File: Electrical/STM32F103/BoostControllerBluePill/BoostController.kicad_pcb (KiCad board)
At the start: 2 copper layers, 81.8 x 80 mm, 57 parts, among them J1 PW-RPM-SPD-TPS, J2 OIL-WATER-AFR, J3 WG-FPUMP, J4 MAP-FPRES, J5 CAN, J6 GND_TP, J7 PROG, Q1 IRF540N, Q2 IRF540N, Q3 BC337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

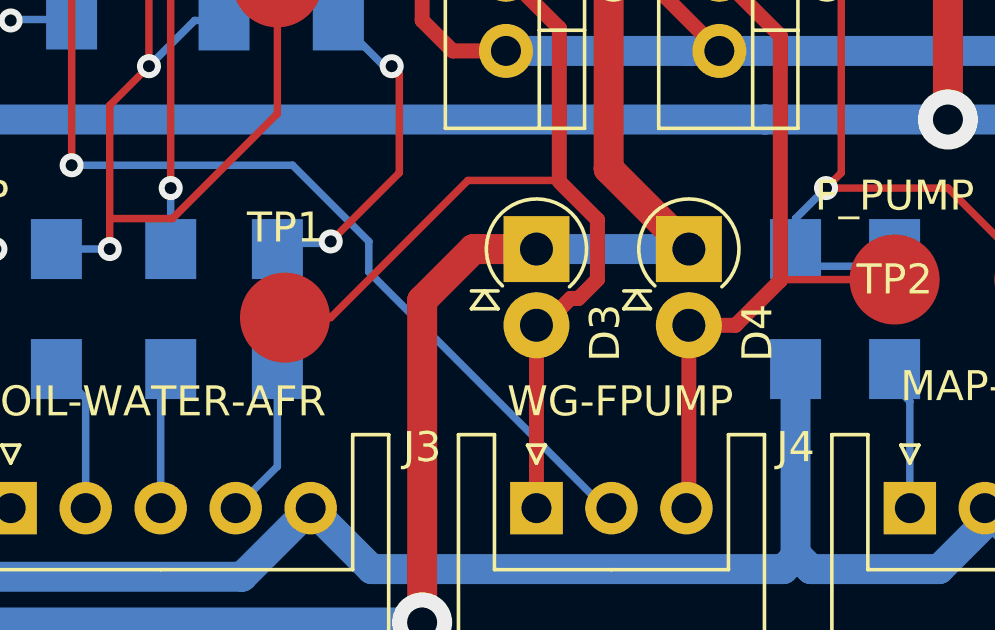
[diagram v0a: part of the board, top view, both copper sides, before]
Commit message: PCB rev 1.1 Fixed track width for solenoid and relay driver Removed spurious hole Cleared overwrites in fab layer Fixed missing name on WG_SOL TP
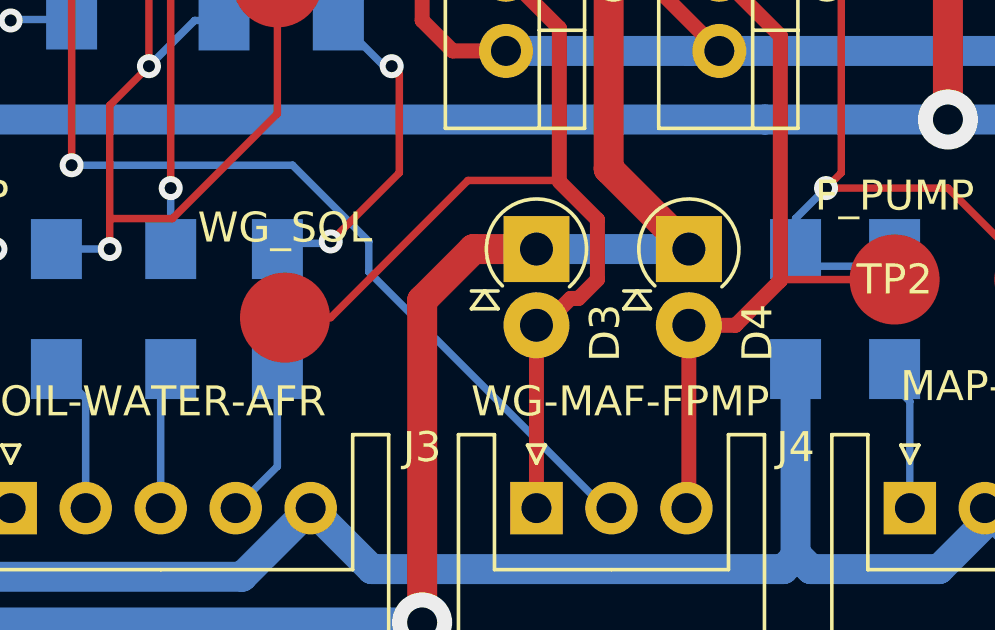
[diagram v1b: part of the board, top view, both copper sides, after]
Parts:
- J3: value WG-FPUMP -> WG-MAF-FPMP
- renumbered TP1 to WG_SOL

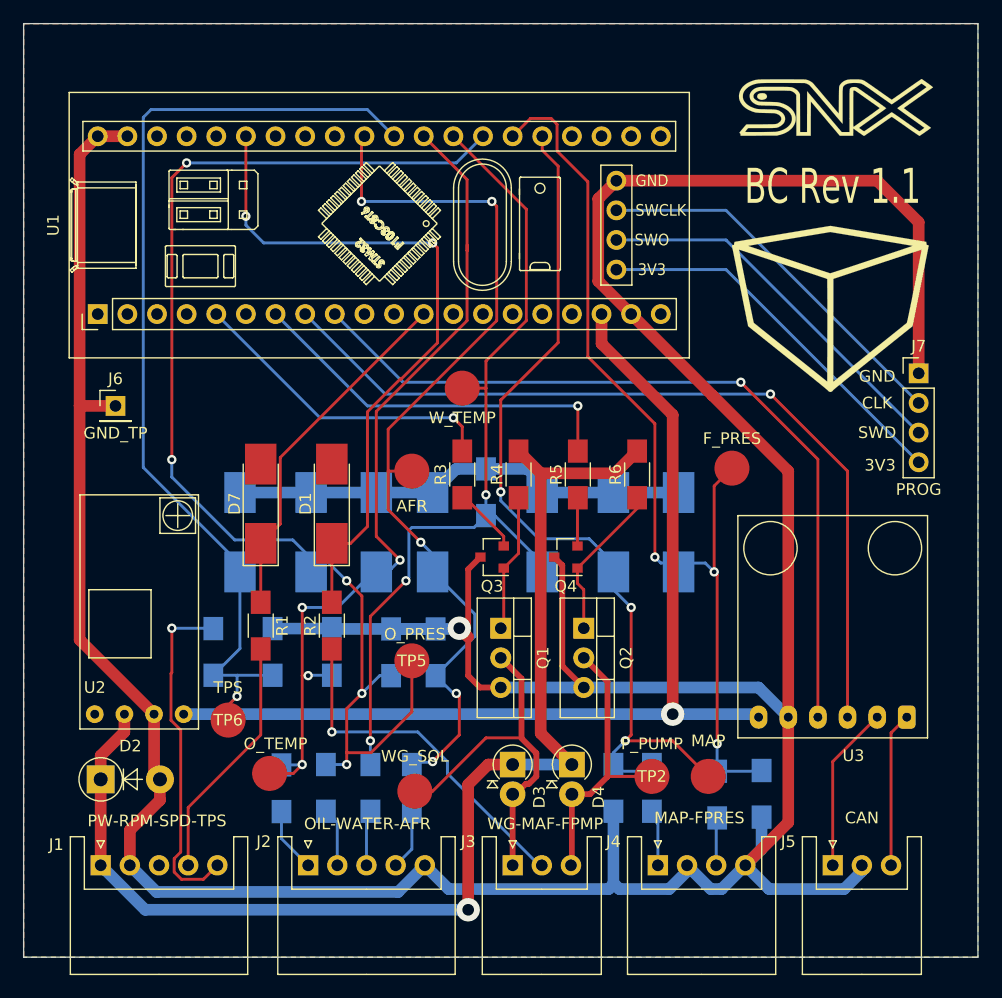
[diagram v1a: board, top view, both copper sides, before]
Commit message: PCB rev 1.2 Fixed missing RPM input Ported to Kicad 6 Fixed DRC warning on silkscreen
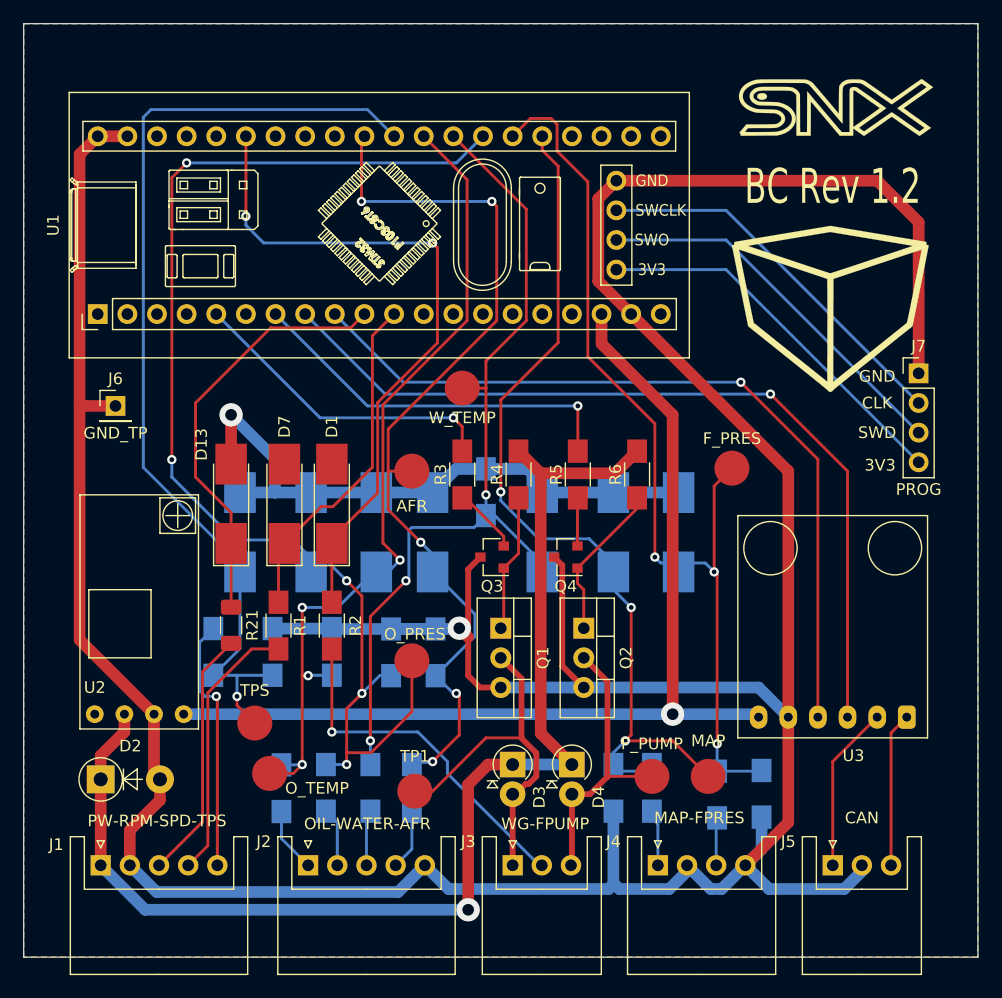
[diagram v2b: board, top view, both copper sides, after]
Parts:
- added D13: 3.3V, Diode_SMD:D_MELF_Handsoldering, F.Cu at (76.2, 85.6)
- added R21: 4.7k, Resistor_SMD:R_1206_3216Metric_Pad1.30x1.75mm_HandSolder, F.Cu at (76.2, 96.0)
- J3: value WG-MAF-FPMP -> WG-FPUMP
- moved TP6 2.30 mm to (78.2, 104.4)
- moved D7 2.03 mm to (80.8, 85.6)
- moved R1 1.52 mm to (80.3, 96.0)
- renumbered WG_SOL to TP1
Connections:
- J1 pad 3: (no net) -> /RPM
- U1 pad 1: (no net) -> unconnected-(U1-Pad1)
- U1 pad 10: (no net) -> Net-(U1-Pad10)
- U1 pad 11: (no net) -> Net-(D7-Pad1)
- U1 pad 12: Net-(D7-Pad1) -> unconnected-(U1-Pad12)
- U1 pad 13: (no net) -> unconnected-(U1-Pad13)
- U1 pad 14: (no net) -> unconnected-(U1-Pad14)
- U1 pad 15: (no net) -> unconnected-(U1-Pad15)
- U1 pad 16: (no net) -> unconnected-(U1-Pad16)
- U1 pad 17: (no net) -> unconnected-(U1-Pad17)
- U1 pad 2: (no net) -> unconnected-(U1-Pad2)
- U1 pad 20: (no net) -> unconnected-(U1-Pad20)
- U1 pad 21: (no net) -> unconnected-(U1-Pad21)
- U1 pad 22: (no net) -> unconnected-(U1-Pad22)
- U1 pad 23: (no net) -> unconnected-(U1-Pad23)
- U1 pad 24: (no net) -> unconnected-(U1-Pad24)
- U1 pad 3: (no net) -> unconnected-(U1-Pad3)
- U1 pad 32: (no net) -> unconnected-(U1-Pad32)
- U1 pad 33: (no net) -> unconnected-(U1-Pad33)
- U1 pad 34: (no net) -> unconnected-(U1-Pad34)
- U1 pad 36: (no net) -> unconnected-(U1-Pad36)
- U1 pad 37: (no net) -> unconnected-(U1-Pad37)
- U1 pad 38: (no net) -> unconnected-(U1-Pad38)
- U1 pad 4: (no net) -> unconnected-(U1-Pad4)
- U1 pad 6: (no net) -> unconnected-(U1-Pad6)
- U2 pad 4: (no net) -> unconnected-(U2-Pad4)
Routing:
- net Net-(U1-Pad10): track 0.00 -> 36.4 mm
- net /RPM: track 0.00 -> 21.6 mm
- net GND: track 375.2 -> 387.6 mm, vias 1 -> 2
- net /TPS: track 29.5 -> 22.0 mm
- net /SPEED: track 21.1 -> 23.1 mm
- net Net-(D7-Pad1): track 30.5 -> 29.4 mm
- net /MAF_33: track 60.0 -> 59.0 mm
- net /OIL_TEMP_33: track 73.4 -> 72.4 mm
- net /TPS_33: track 84.2 -> 84.7 mm
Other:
- net class Default removed
- net class Power removed
- board text added: "BC Rev 1.2"
- board text removed: "BC Rev 1.1"

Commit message: Fixed SOT-23 transistors. Added test points. Changed footprint to Kicad6.
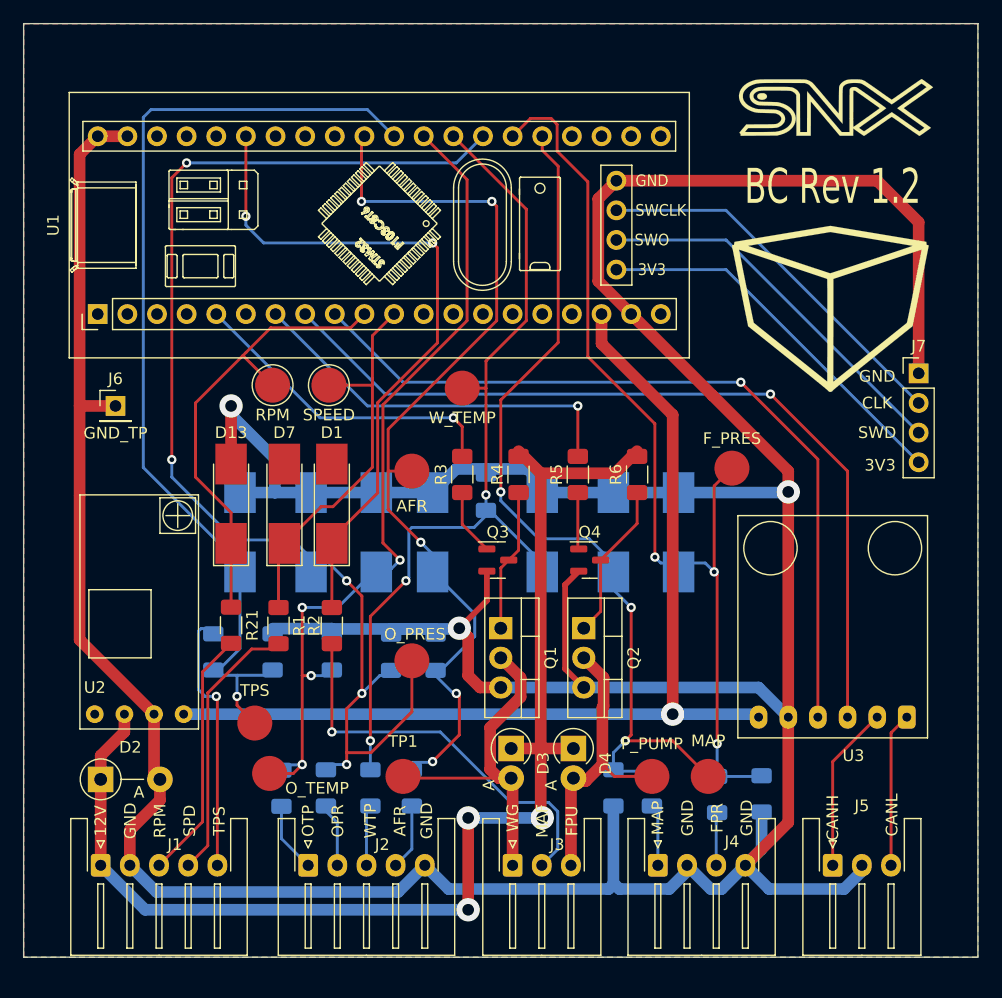
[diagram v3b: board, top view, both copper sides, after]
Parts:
- added TP10: RPM, TestPoint:TestPoint_Pad_D3.0mm, F.Cu at (79.8, 75.4)
- added TP11: SPEED, TestPoint:TestPoint_Pad_D3.0mm, F.Cu at (84.6, 75.4)
- D1, D10, D11, D5, D6, D7, D8, D9: footprint Diodes_SMD:D_MELF_Handsoldering -> Diode_SMD:D_MELF_Handsoldering
- D2: footprint Diodes_THT:D_DO-15_P5.08mm_Vertical_AnodeUp -> Diode_THT:D_DO-41_SOD81_P5.08mm_Vertical_AnodeUp
- D3, D4: footprint Diodes_THT:D_DO-41_SOD81_P2.54mm_Vertical_AnodeUp -> Diode_THT:D_DO-41_SOD81_P2.54mm_Vertical_AnodeUp
- J1, J2: footprint Connectors_JST:JST_XH_S05B-XH-A_05x2.50mm_Angled -> Connector_JST:JST_XH_S5B-XH-A-1_1x05_P2.50mm_Horizontal
- J3, J5: footprint Connectors_JST:JST_XH_S03B-XH-A_03x2.50mm_Angled -> Connector_JST:JST_XH_S3B-XH-A-1_1x03_P2.50mm_Horizontal
- J4: footprint Connectors_JST:JST_XH_S04B-XH-A_04x2.50mm_Angled -> Connector_JST:JST_XH_S4B-XH-A-1_1x04_P2.50mm_Horizontal
- J7: footprint Pin_Headers:Pin_Header_Straight_1x04_Pitch2.54mm -> Connector_PinHeader_2.54mm:PinHeader_1x04_P2.54mm_Vertical
- Q1, Q2: footprint TO_SOT_Packages_THT:TO-220-3_Vertical -> Package_TO_SOT_THT:TO-220-3_Vertical
- Q3, Q4: value BC337 -> S9013; footprint TO_SOT_Packages_SMD:SOT-23 -> Package_TO_SOT_SMD:SOT-23
- R1, R10, R11, R12, R13, R14, R15, R16, R17, R18, R19, R2, R20, R3, R4, R5, R6, R7, R8, R9: footprint Resistors_SMD:R_1206_HandSoldering -> Resistor_SMD:R_1206_3216Metric_Pad1.30x1.75mm_HandSolder
- moved Q4 2.06 mm to (106.9, 90.4), turned to 0 degrees
- moved TP1 1.63 mm to (90.9, 109.0)
- moved D4 1.38 mm to (105.5, 106.6)
- moved D3 1.38 mm to (100.2, 106.6)
- moved Q3 0.55 mm to (99.1, 90.4), turned to 0 degrees
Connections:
- Q3 pad 1: Net-(Q1-Pad1) -> Net-(R3-Pad1)
- Q3 pad 2: Net-(Q3-Pad2) -> GND
- Q3 pad 3: GND -> Net-(Q1-Pad1)
- Q4 pad 1: Net-(Q2-Pad1) -> Net-(R5-Pad1)
- Q4 pad 2: Net-(Q4-Pad2) -> GND
- Q4 pad 3: GND -> Net-(Q2-Pad1)
- R3 pad 1: Net-(Q3-Pad2) -> Net-(R3-Pad1)
- R5 pad 1: Net-(Q4-Pad2) -> Net-(R5-Pad1)
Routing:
- net GND: track 387.6 -> 395.5 mm, vias 2 -> 3
- net Net-(Q3-Pad2): track 5.86 -> 0.00 mm
- net Net-(R3-Pad1): track 0.00 -> 5.26 mm
- net Net-(R5-Pad1): track 0.00 -> 4.42 mm
- net Net-(Q4-Pad2): track 4.14 -> 0.00 mm
- net /MAF: track 30.4 -> 34.5 mm
- net Net-(D7-Pad1): track 29.4 -> 33.2 mm
- net Net-(D13-Pad1): track 36.4 -> 40.0 mm
- net +12V: track 105.0 -> 107.8 mm, vias 1 -> 3
- net /MAP: track 4.27 -> 5.30 mm
- net /WG_SOL: track 31.2 -> 30.3 mm
- net /TPS: track 22.0 -> 22.7 mm
- net /F_PRES_33: track 81.4 -> 81.9 mm
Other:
- board text added: "12V"
- board text added: "AFR"
- board text added: "CANH"
- board text added: "CANL"
- board text added: "FPR"
- board text added: "FPU"
- board text added: "MAF"
- board text added: "MAP"
- board text added: "OPR"
- board text added: "OTP"
- board text added: "RPM"
- board text added: "SPD"
- board text added: "TPS"
- board text added: "WG"
- board text added: "WTP"

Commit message: Fixed D12 footprint
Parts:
- D12: footprint Diodes_SMD:D_MELF_Handsoldering -> Diode_SMD:D_MELF_Handsoldering

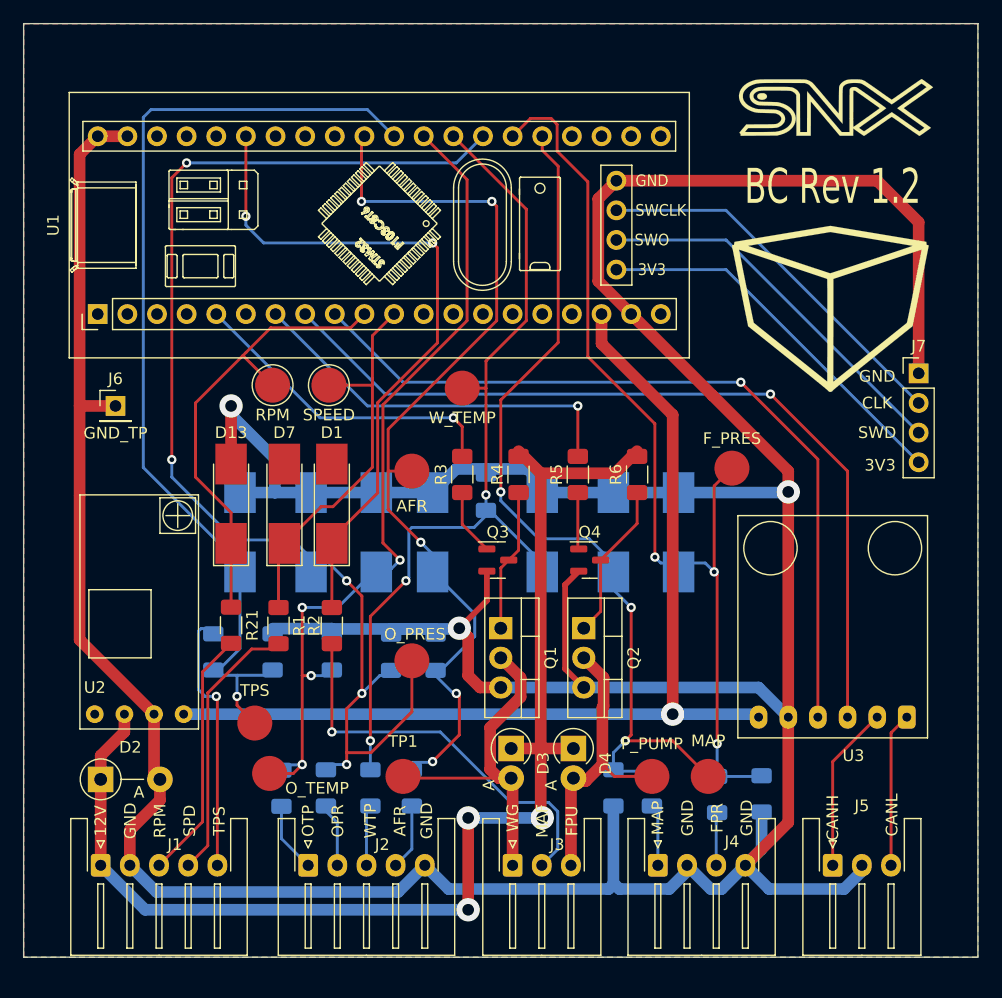
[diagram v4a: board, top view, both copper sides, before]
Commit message: Replaced Zener protectio diode (that did not work as expected) with capacitor filter. Replaced MOSFET reference. Clarification on schematic. Changed analog voltage divider resistor values. Added missing test point for MAF input.
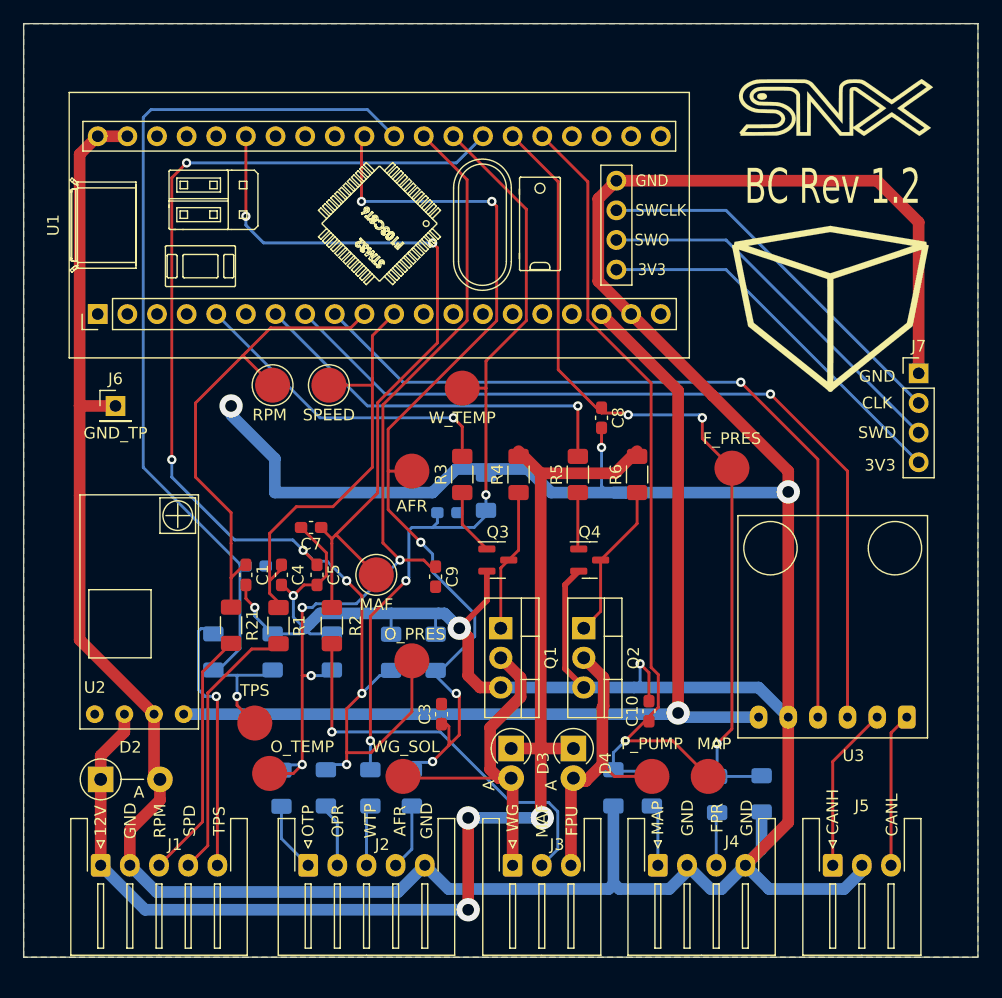
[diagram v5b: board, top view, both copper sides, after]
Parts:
- removed D1, D10, D11, D12, D13, D5, D6, D7, D8, D9: 3.3V, Diode_SMD:D_MELF_Handsoldering
- added C1: 10n, Capacitor_SMD:C_0603_1608Metric_Pad1.08x0.95mm_HandSolder, F.Cu at (77.5, 91.7)
- added C10: 10µ, Capacitor_SMD:C_0603_1608Metric_Pad1.08x0.95mm_HandSolder, F.Cu at (112.0, 103.4)
- added C2: 10µ, Capacitor_SMD:C_0603_1608Metric_Pad1.08x0.95mm_HandSolder, B.Cu at (94.7, 86.4)
- added C3: 10µ, Capacitor_SMD:C_0603_1608Metric_Pad1.08x0.95mm_HandSolder, F.Cu at (94.2, 103.6)
- added C4: 10n, Capacitor_SMD:C_0603_1608Metric_Pad1.08x0.95mm_HandSolder, F.Cu at (80.5, 91.7)
- added C5: 10µ, Capacitor_SMD:C_0603_1608Metric_Pad1.08x0.95mm_HandSolder, F.Cu at (83.6, 91.7)
- added C6: 10µ, Capacitor_SMD:C_0603_1608Metric_Pad1.08x0.95mm_HandSolder, B.Cu at (78.3, 90.9)
- added C7: 10n, Capacitor_SMD:C_0603_1608Metric_Pad1.08x0.95mm_HandSolder, F.Cu at (83.1, 87.6)
- added C8: 10µ, Capacitor_SMD:C_0603_1608Metric_Pad1.08x0.95mm_HandSolder, F.Cu at (108.0, 78.2)
- added C9: 10µ, Capacitor_SMD:C_0603_1608Metric_Pad1.08x0.95mm_HandSolder, F.Cu at (93.7, 91.8)
- added TP12: MAF, TestPoint:TestPoint_Pad_D3.0mm, F.Cu at (88.6, 91.7)
- Q1, Q2: value IRF540N -> IRF3205
- R10, R12, R14, R16, R18, R20, R8: value 3.3k -> 2.2k
- R11, R13, R15, R17, R19, R7, R9: value 1.7k -> 1.2k
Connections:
- net Net-(D13-Pad1) renamed /RPM_33
- net Net-(D7-Pad1) renamed /SPEED_33
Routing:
- net GND: track 395.5 -> 421.9 mm, vias 3 -> 7
- net /F_PRES_33: track 81.9 -> 71.9 mm
- net /MAF_33: track 59.0 -> 65.2 mm
- net /WATER_TEMP_33: track 73.5 -> 68.4 mm
- net /MAP_33: track 75.7 -> 72.0 mm, vias 3 -> 1
- net /OIL_TEMP_33: track 72.4 -> 75.9 mm
- net /SPEED_33: track 33.2 -> 36.4 mm
- net /AFR_33: track 79.1 -> 81.7 mm
- net /OIL_PRES_33: track 105.6 -> 107.4 mm, vias 5 -> 6
- net /RPM_33: track 40.0 -> 41.7 mm
